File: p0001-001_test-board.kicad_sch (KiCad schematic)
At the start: 5 parts

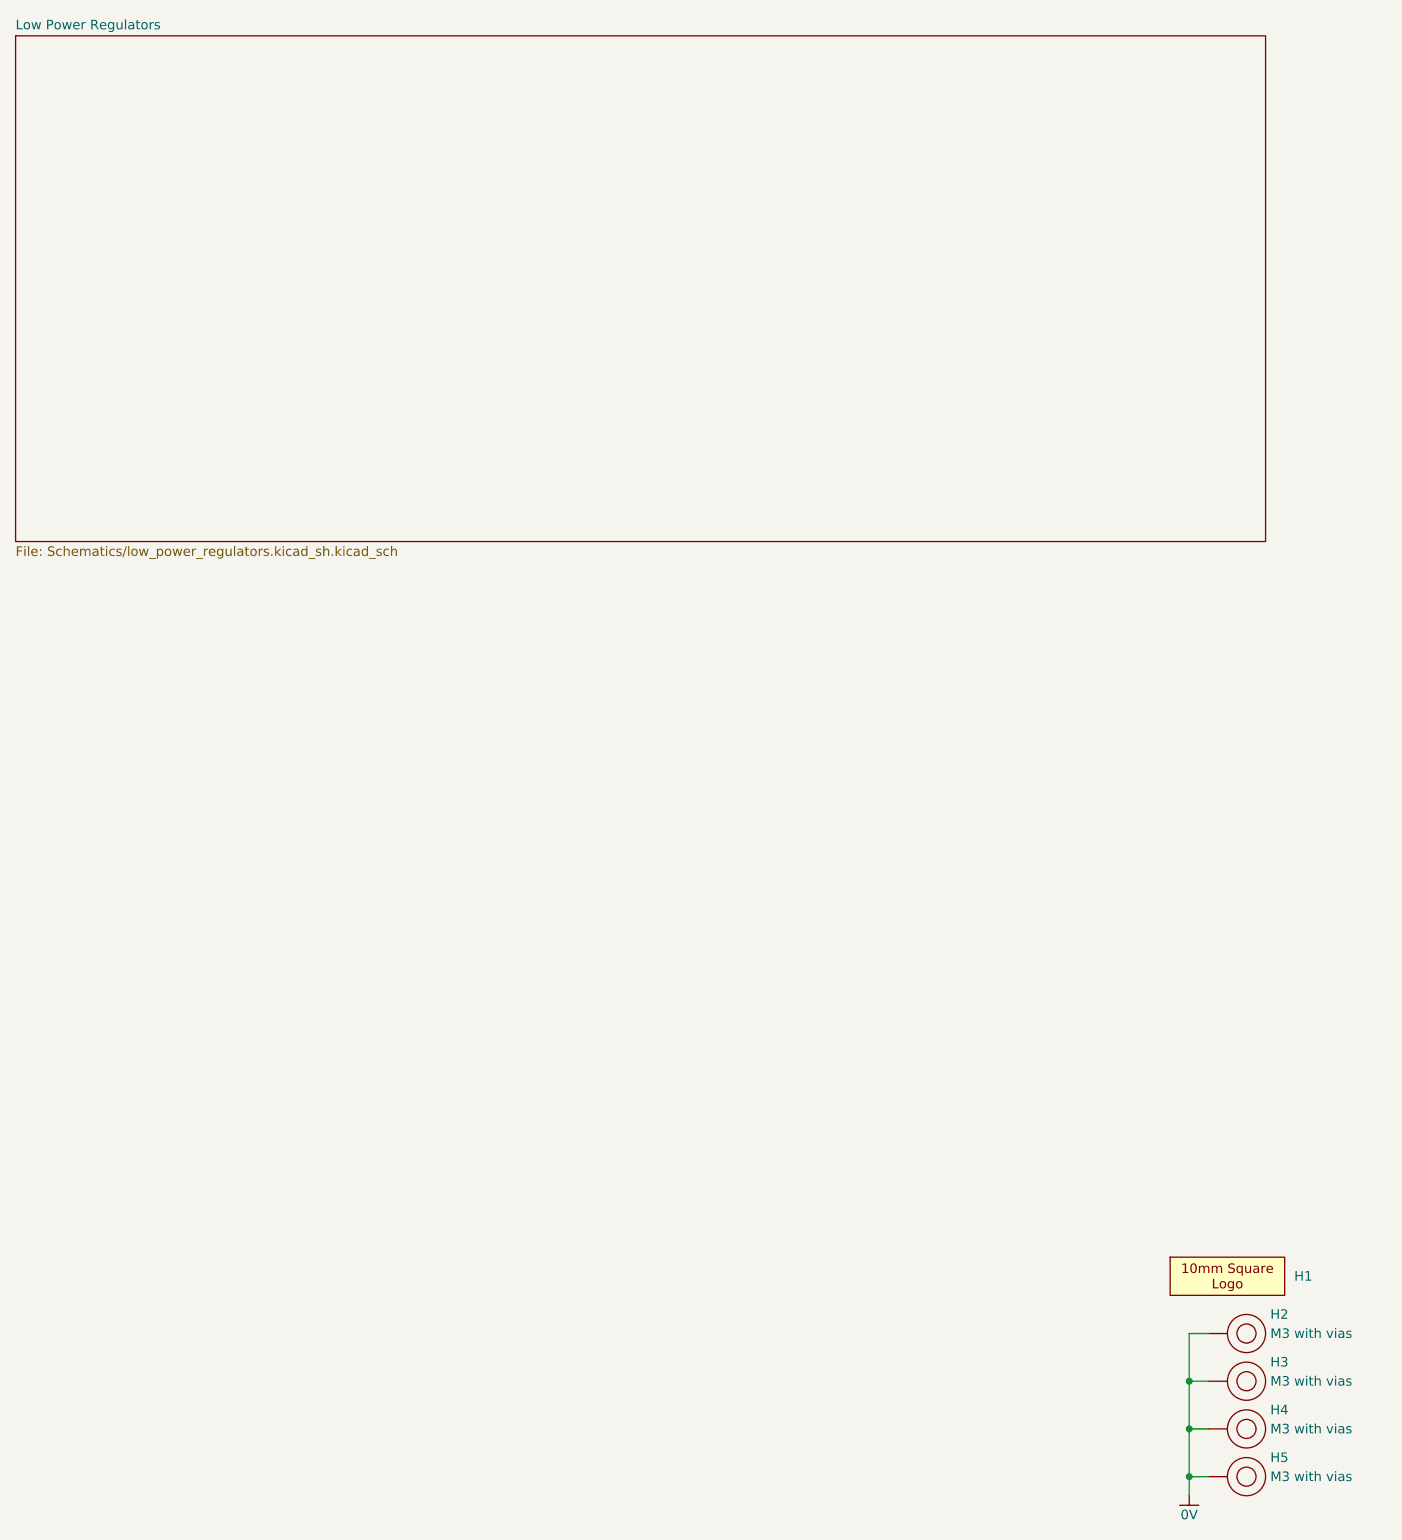
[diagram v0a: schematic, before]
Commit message: It is a root page bug. Trying with preferred font
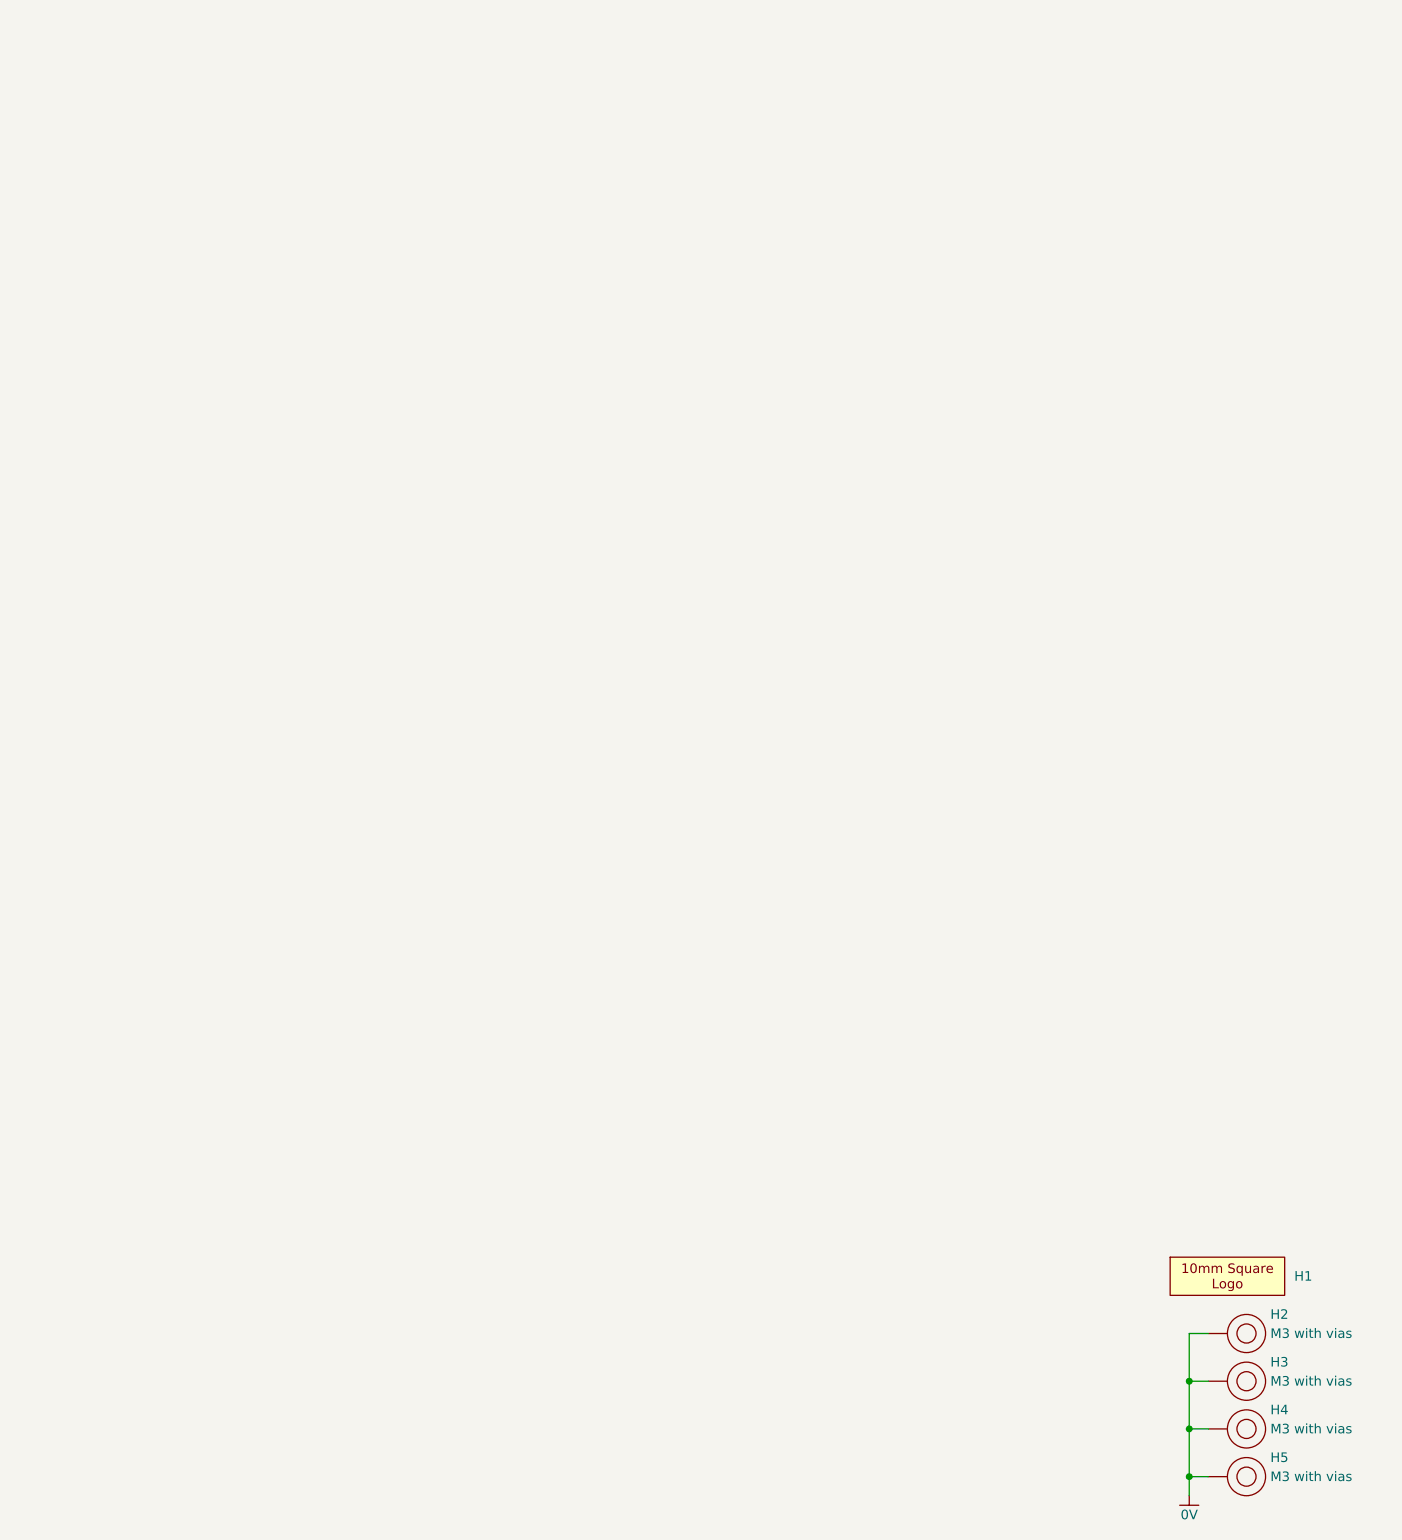
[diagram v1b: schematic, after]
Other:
- removed sheet Low Power Regulators
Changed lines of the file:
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@@
-		)
-	)
-	(sheet
-		(at 106.68 83.82)
-		(size 166.37 67.31)
-		(exclude_from_sim no)
-		(in_bom yes)
-		(on_board yes)
-		(dnp no)
-		(fields_autoplaced yes)
-		(stroke
-			(width 0.1524)
-			(type solid)
-		)
-		(fill
-			(color 0 0 0 0)
-		)
-		(property "Sheetname" "Low Power Regulators"
-			(at 106.68 83.1084 0)
-			(show_name no)
-			(do_not_autoplace no)
-			(effects
-				(font
-					(size 1.27 1.27)
-				)
-				(justify left bottom)
-			)
-		)
-		(property "Sheetfile" "Schematics/low_power_regulators.kicad_sh.kicad_sch"
-			(at 106.68 151.7146 0)
-			(show_name no)
-			(do_not_autoplace no)
-			(effects
-				(font
-					(size 1.27 1.27)
-				)
-				(justify left top)
-			)
-		)
-		(instances
-			(project "p0001-001_test-board"
-				(path "/acdb93e6-9aa6-4a78-8a68-9d0ae3318f45"
-					(page "2")
-				)
-			)
 		)
 	)

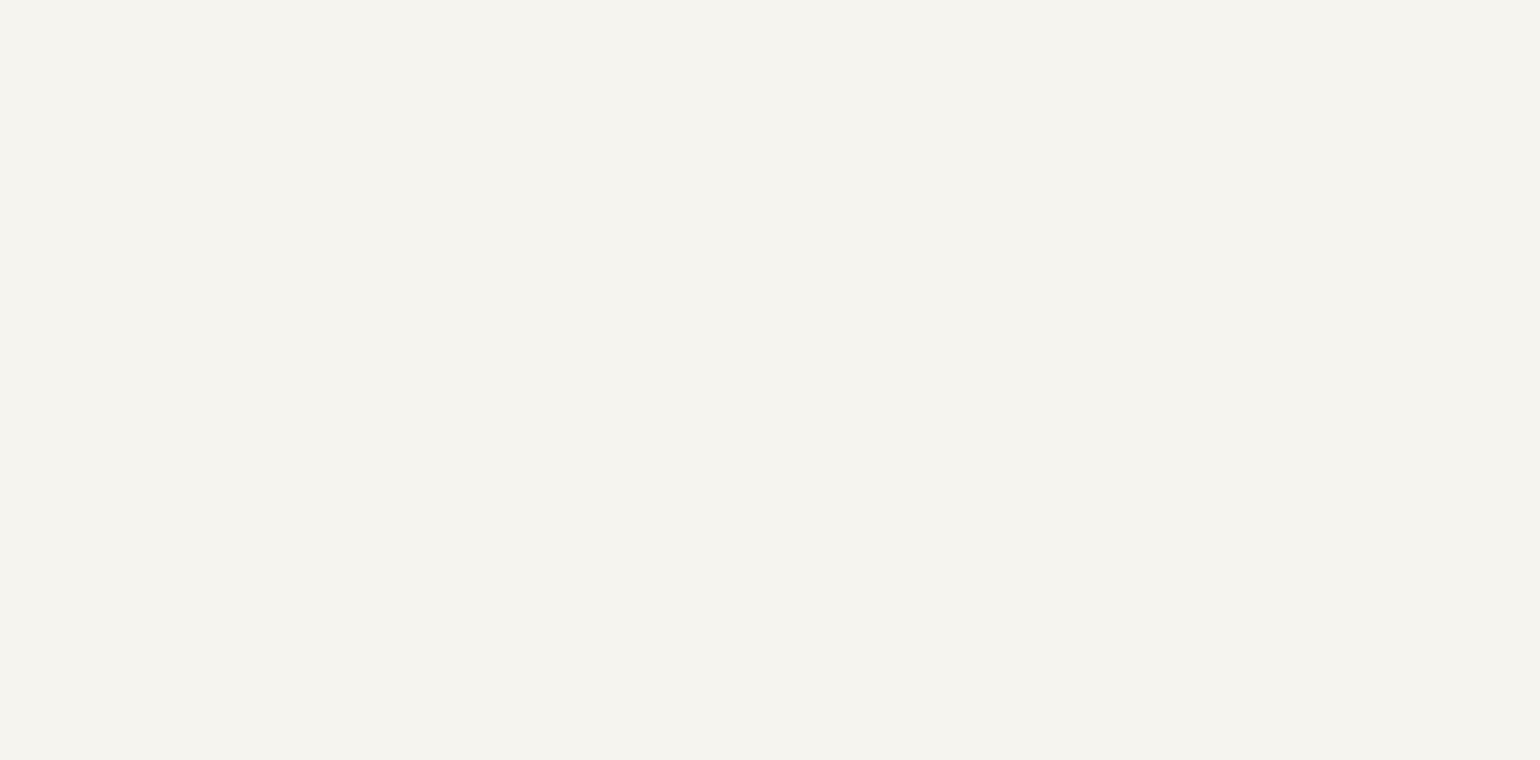
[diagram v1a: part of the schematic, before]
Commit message: somehow deleted child sheet in process
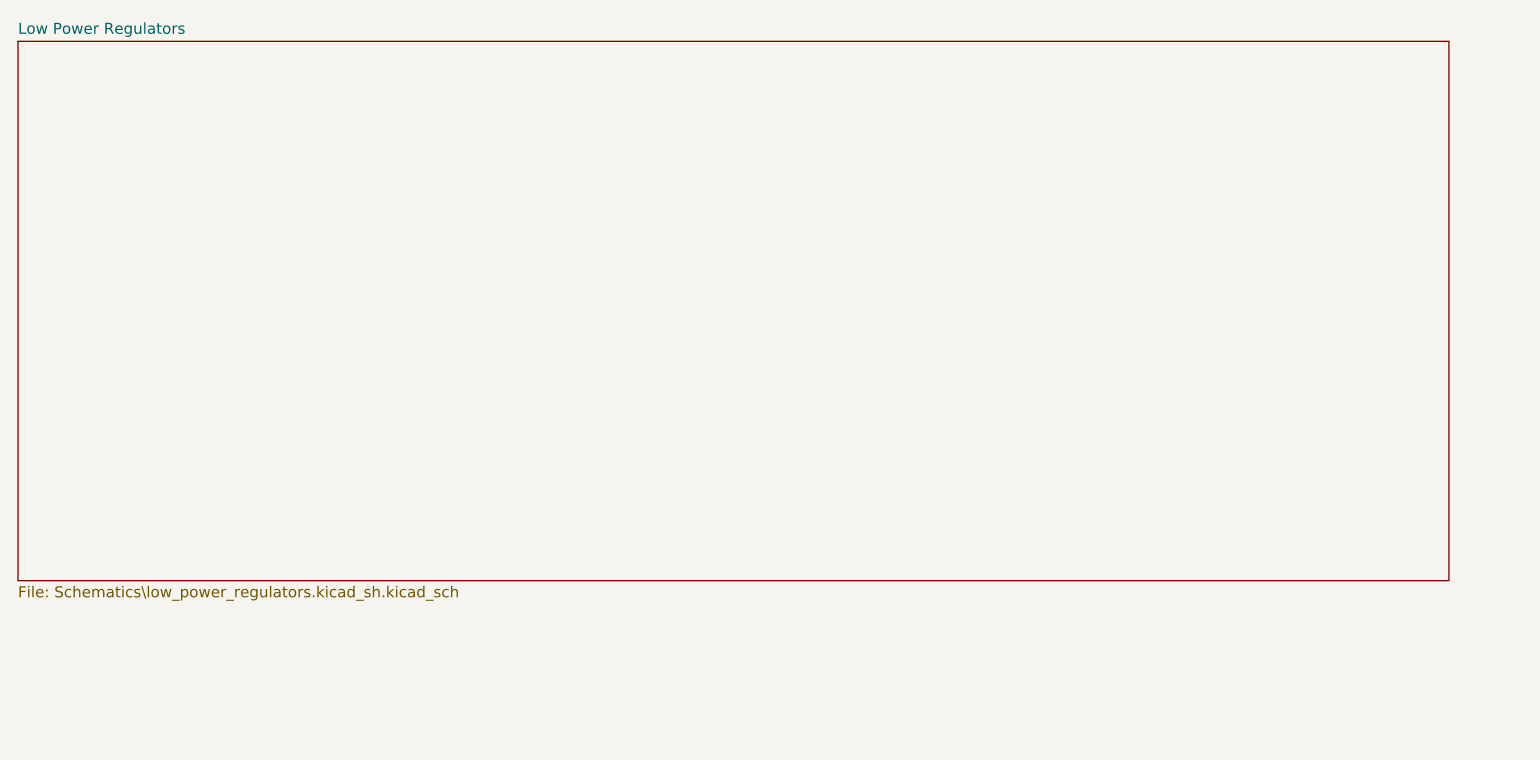
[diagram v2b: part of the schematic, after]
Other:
- added sheet Low Power Regulators (Schematics\low_power_regulators.kicad_sh.kicad_sch)
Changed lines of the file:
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@@
+		)
+	)
+	(sheet
+		(at 115.57 102.87)
+		(size 165.1 62.23)
+		(exclude_from_sim no)
+		(in_bom yes)
+		(on_board yes)
+		(dnp no)
+		(fields_autoplaced yes)
+		(stroke
+			(width 0.1524)
+			(type solid)
+		)
+		(fill
+			(color 0 0 0 0)
+		)
+		(property "Sheetname" "Low Power Regulators"
+			(at 115.57 102.1584 0)
+			(show_name no)
+			(do_not_autoplace no)
+			(effects
+				(font
+					(size 1.27 1.27)
+				)
+				(justify left bottom)
+			)
+		)
+		(property "Sheetfile" "Schematics\\low_power_regulators.kicad_sh.kicad_sch"
+			(at 115.57 165.6846 0)
+			(show_name no)
+			(do_not_autoplace no)
+			(effects
+				(font
+					(size 1.27 1.27)
+				)
+				(justify left top)
+			)
+		)
+		(instances
+			(project "p0001-001_test-board"
+				(path "/acdb93e6-9aa6-4a78-8a68-9d0ae3318f45"
+					(page "2")
+				)
+			)
 		)
 	)
